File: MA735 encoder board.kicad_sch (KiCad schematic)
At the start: 4 parts, among them J1 FPC contacts 0.3mm, U1 MA735GGU-Z

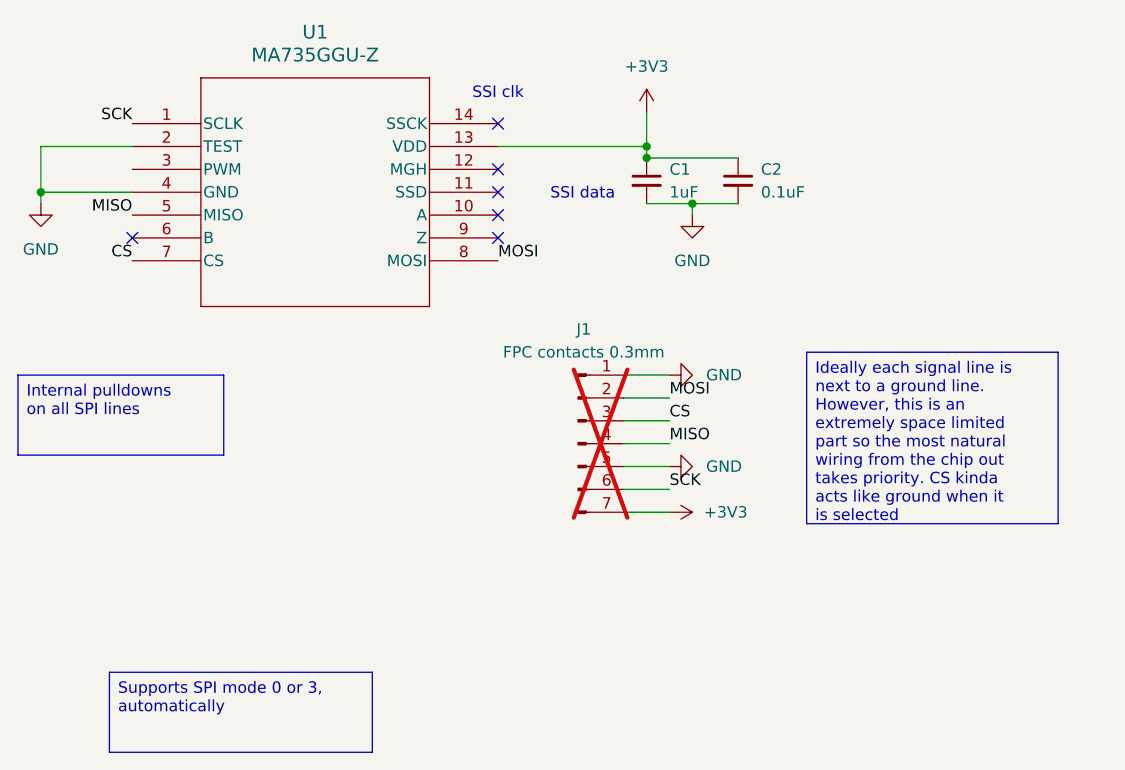
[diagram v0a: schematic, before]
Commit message: Tweaked schematic layout to be slightly less jank
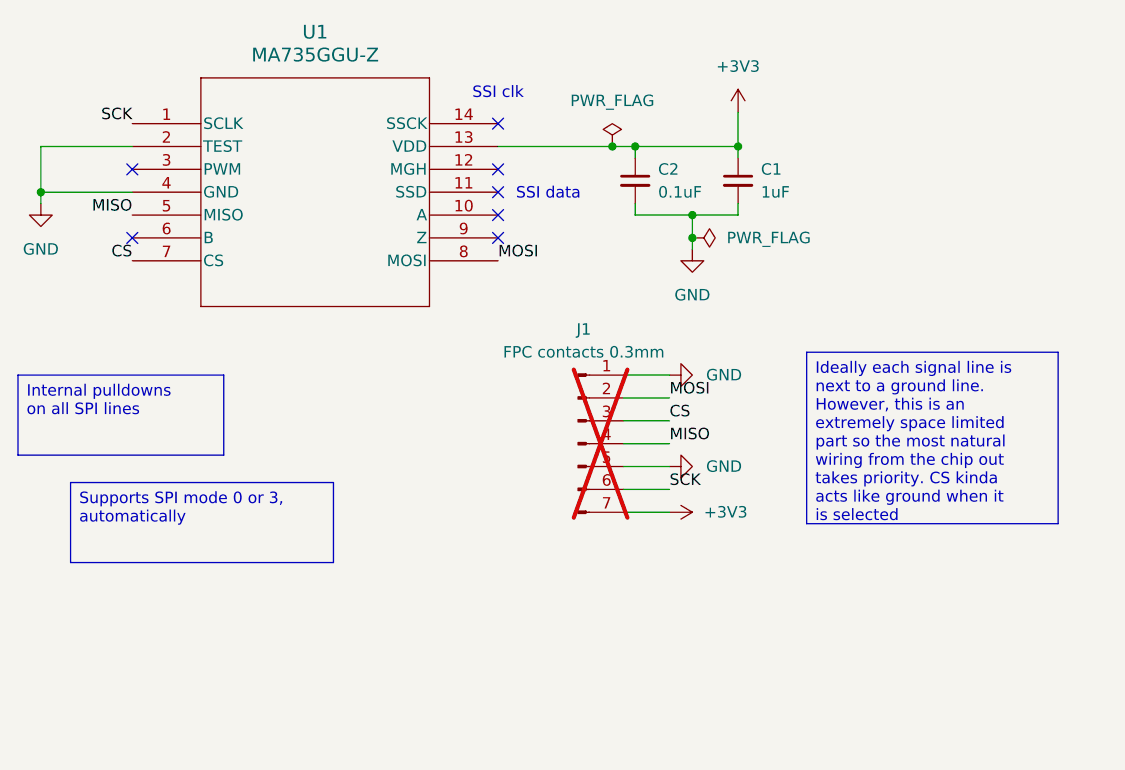
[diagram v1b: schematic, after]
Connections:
- no-connect marks 6 -> 7
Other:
- moved on the sheet: C1, C2
